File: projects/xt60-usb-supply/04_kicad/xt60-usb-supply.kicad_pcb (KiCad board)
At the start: 4 copper layers, 92 x 62 mm, 51 parts, among them J1 XT60PW-M, J2 USB-A, J3 USB-A, J4 USB-A, J5 TYPE-C-31-M-12A, Q1 AOD4185, U1 SY8368QNC, U2 SY8368QNC, U3 USBLC6-2SC6, U4 USBLC6-2SC6, U5 USBLC6-2SC6, U6 USBLC6-2SC6

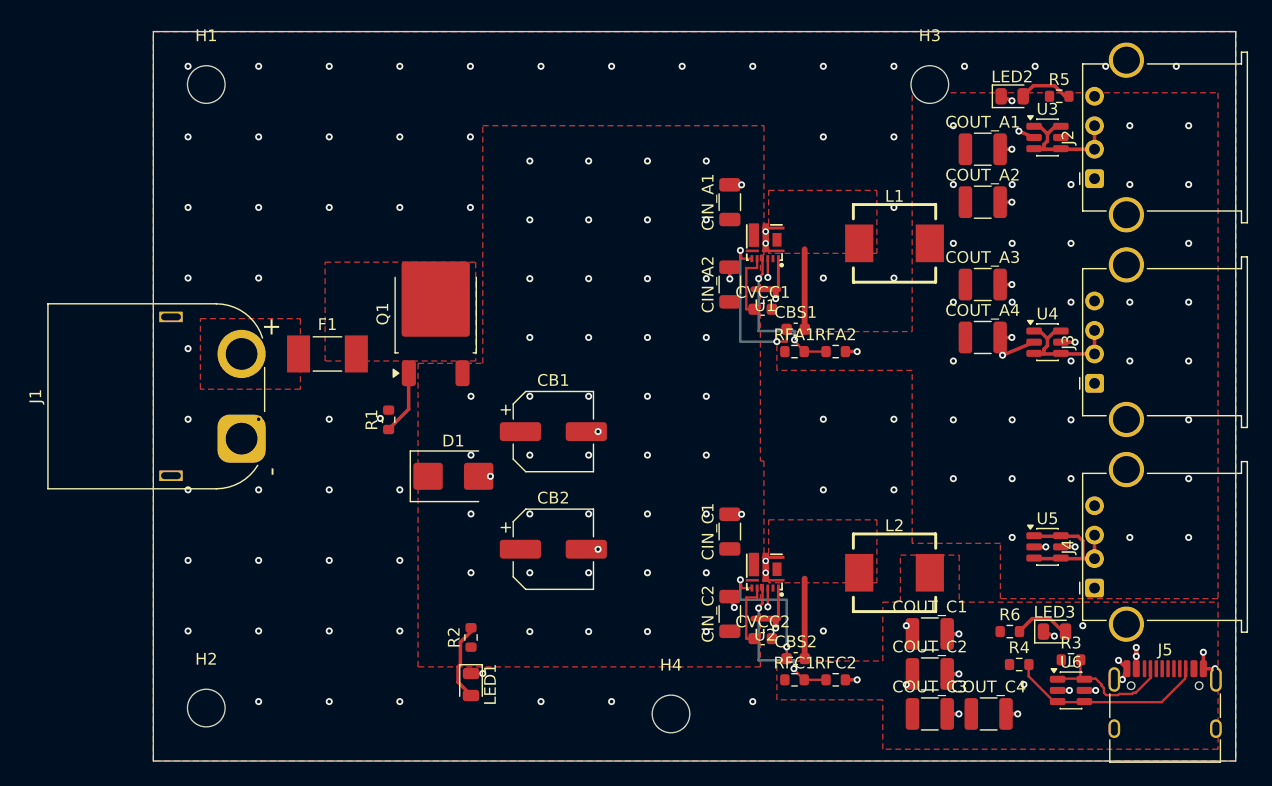
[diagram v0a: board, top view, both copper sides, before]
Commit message: xt60-usb-supply: review triage — USB-C BC1.2 DCP short (ADR 0008), U3 VBUS rescue, hidden H refs; gate green again; fab agent artifacts (2.2uF part, twin adjudications, fab outputs)
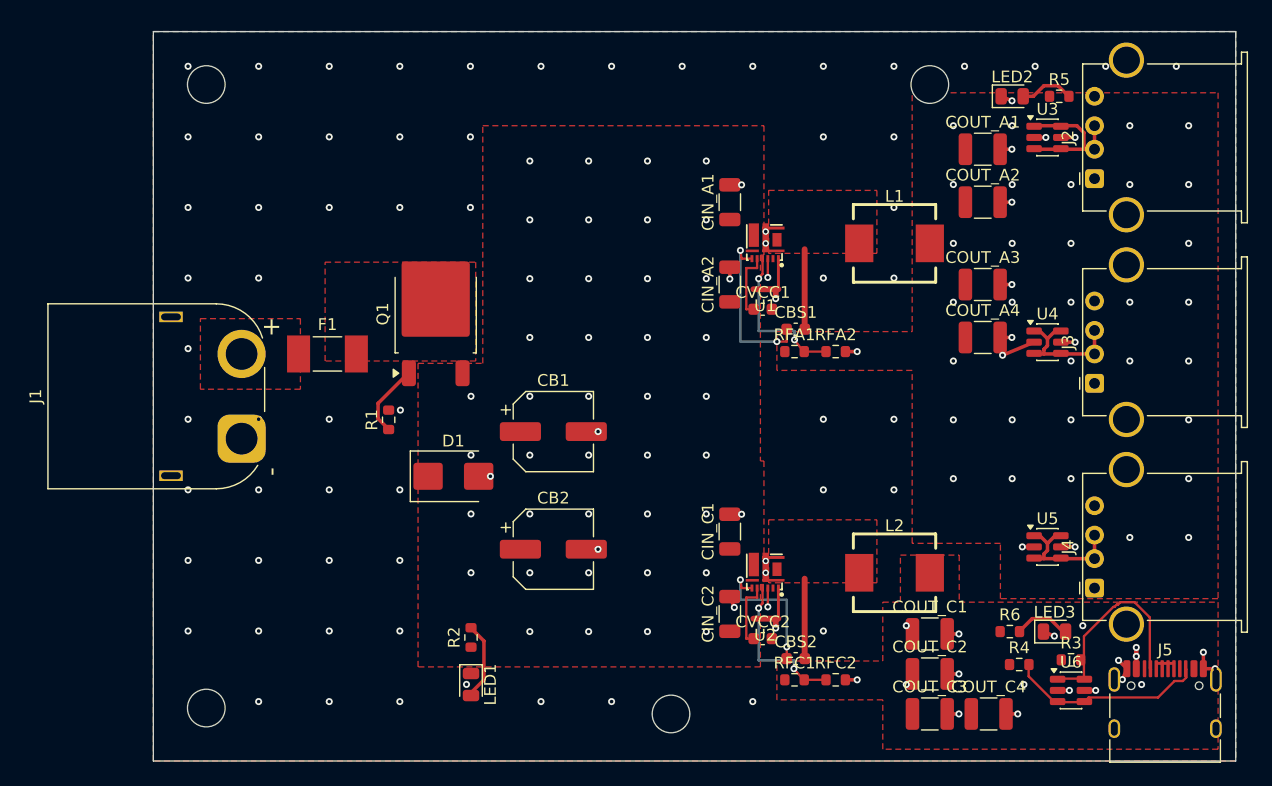
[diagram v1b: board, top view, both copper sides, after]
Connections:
- J5 pad A6: NC_J5_A6 -> DCPC
- J5 pad A7: NC_J5_A7 -> DCPC
- J5 pad B6: NC_J5_B6 -> DCPC
- J5 pad B7: NC_J5_B7 -> DCPC
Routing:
- net CC1: track 11.9 -> 18.1 mm
- net DCP3: track 13.1 -> 11.5 mm
- net DCP1: track 11.6 -> 13.2 mm
- net DCPC: track 0.00 -> 1.50 mm
- net 5V_A: track 2.43 -> 3.64 mm, vias 13 -> 23
- net PFET_G: track 5.57 -> 6.32 mm
- net GND: track 32.9 -> 32.5 mm, vias 137 -> 127
- net 5V_C: vias 6 -> 8

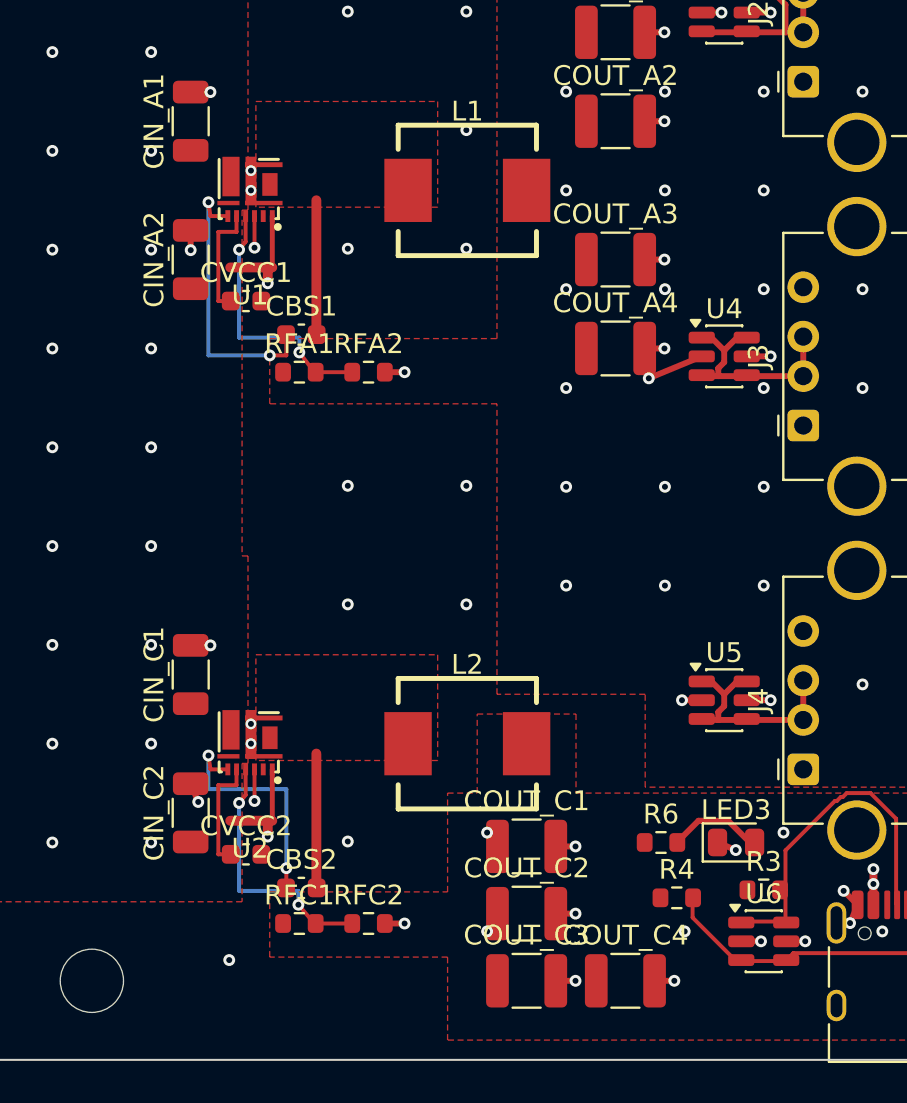
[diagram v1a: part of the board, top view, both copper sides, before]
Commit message: xt60-usb-supply: silk refdes de-collide; fab package refreshed (BOM/CPL stable)
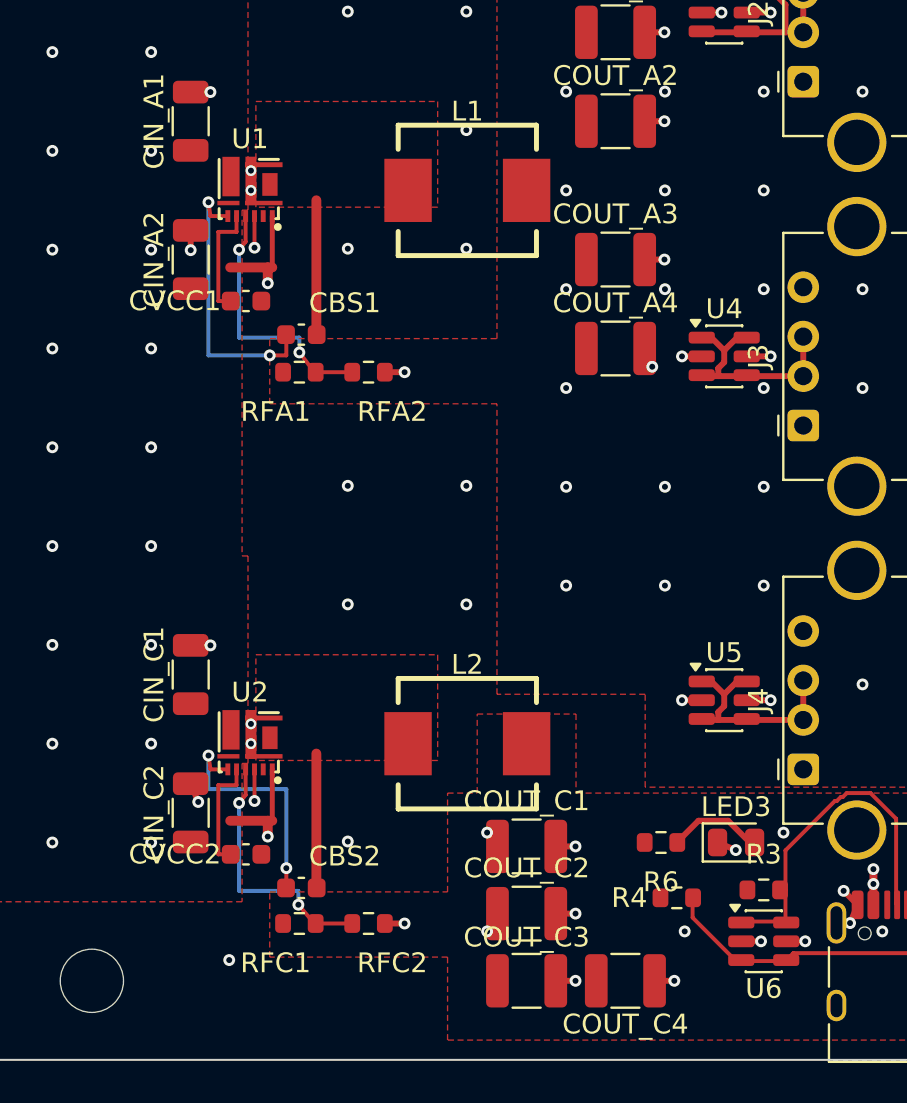
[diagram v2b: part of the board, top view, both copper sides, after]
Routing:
- net GND: track 32.5 -> 30.6 mm, vias 127 -> 129
- net 5V_C: vias 8 -> 6
